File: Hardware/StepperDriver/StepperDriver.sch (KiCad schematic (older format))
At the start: 13 parts, among them M1A CONN_01X02, Q1 FQP20N06, Q2 FQP20N06, Q3 FQP20N06, Q4 FQP20N06, Q5 BC547, Q6 BC547, U1 74HC00

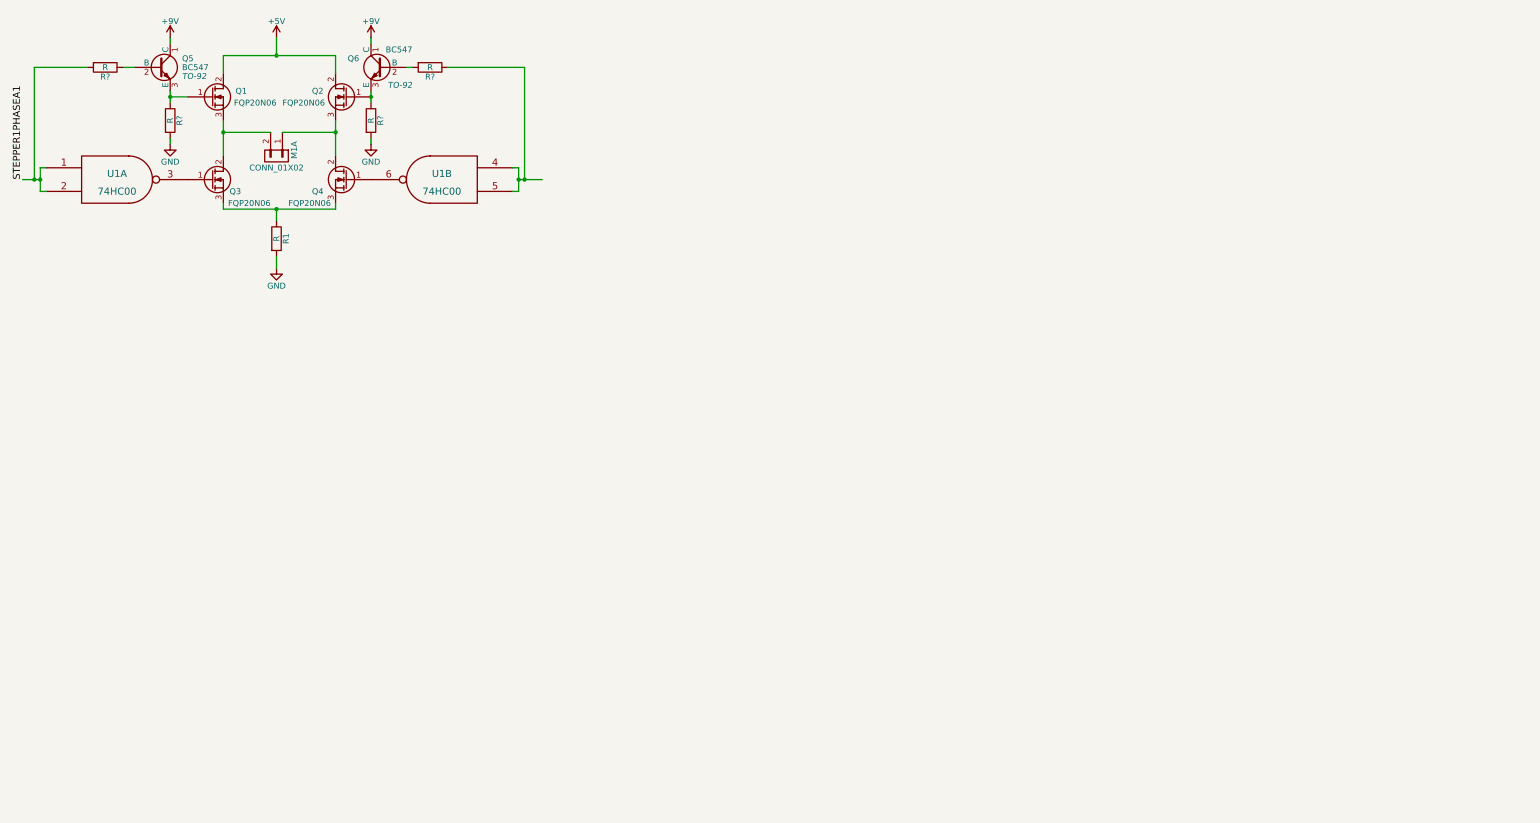
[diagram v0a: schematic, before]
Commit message: updated schematic for 2 motors
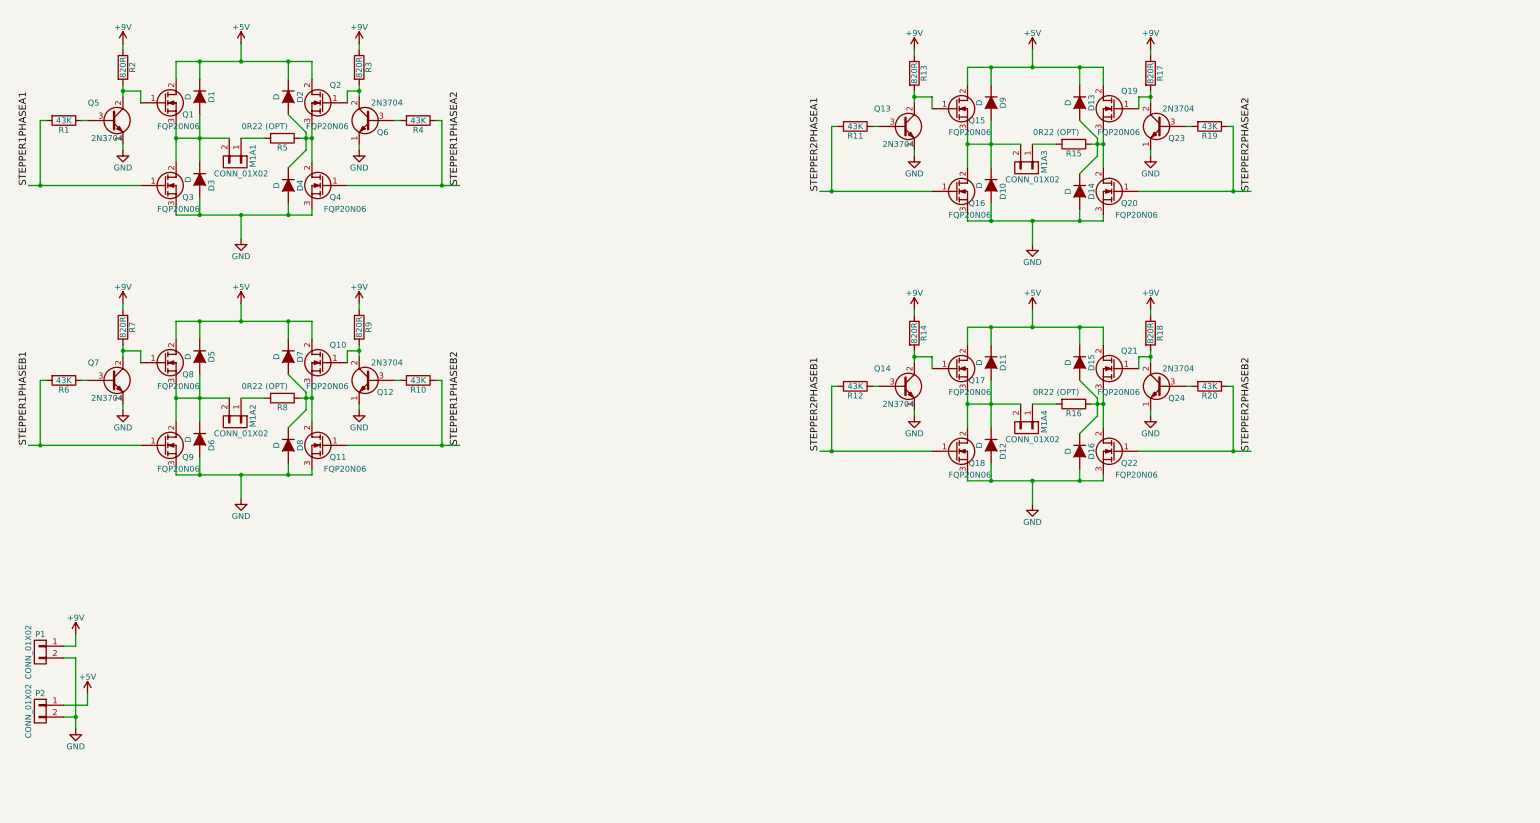
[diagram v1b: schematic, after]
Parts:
- removed Q5, Q6: BC547, TO-92, symbol BC547
- removed U1: 74HC00, symbol 74HC00
- added D1, D10, D11, D12, D13, D14, D15, D16, D2, D3, D4, D5, D6, D7, D8, D9: D, symbol D
- added M1A2, M1A3, M1A4, P1, P2: CONN_01X02, symbol CONN_01X02
- added Q10, Q11, Q15, Q16, Q17, Q18, Q19, Q20, Q21, Q22, Q8, Q9: FQP20N06, symbol Q_NMOS_GDS
- added Q12, Q13, Q14, Q23, Q24, Q5, Q6, Q7: 2N3704, symbol Q_NPN_ECB
- added R10, R11, R12, R19, R20, R6: 43K, symbol R
- added R13, R14, R17, R18, R7, R9: 820R, symbol R
- added R15, R16, R8: 0R22 (OPT), symbol R
- R1, R4: renamed from R?; value R -> 43K
- R2, R3: renamed from R?; value R -> 820R
- R5: renamed from R1; value R -> 0R22 (OPT)
- renumbered M1A to M1A1
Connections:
- net +5V: now also D1.1 (K), D11.1 (K), D13.1 (K), D15.1 (K), D2.1 (K), D5.1 (K), D7.1 (K), D9.1 (K), P2.1 (P1), Q10.2 (D), Q15.2 (D), Q17.2 (D), Q19.2 (D), Q21.2 (D), Q8.2 (D)
- net +9V: now also R2.1, R3.1, P1.1 (P1), R13.1, R14.1, R17.1, R18.1, R7.1, R9.1
- net GND: now also Q3.3 (S), Q4.3 (S), D10.2 (A), D12.2 (A), D14.2 (A), D16.2 (A), D3.2 (A), D4.2 (A), D6.2 (A), D8.2 (A), P1.2 (P2), P2.2 (P2), Q11.3 (S), Q12.1 (E), Q13.1 (E), Q14.1 (E), Q16.3 (S), Q18.3 (S), Q20.3 (S), Q22.3 (S), Q23.1 (E), Q24.1 (E), Q5.1 (E), Q6.1 (E), Q7.1 (E), Q9.3 (S); no longer R2.2, R3.2, R5.2
- net STEPPER1PHASEA1: now also Q3.1 (G)
- net at Q1.1 (G): now also R2.2, Q5.2 (C); no longer R2.1
- net at M1A1.2 (P2), Q1.3 (S), Q3.2 (D): now also D1.2 (A), D3.1 (K)
- net at Q2.1 (G): now also R3.2, Q6.2 (C); no longer R3.1
- net at Q2.3 (S), Q4.2 (D): now also R5.1, D2.2 (A), D4.1 (K); no longer M1A1.1 (P1)
- net STEPPER1PHASEA2: now reaches Q4.1 (G)
- net STEPPER1PHASEA2: now also R4.1
- net at R1.1: now also Q5.3 (B)
- net at R4.2: now also Q6.3 (B)
- new net: M1A1.1 (P1), R5.2
- new net: Q7.2 (C), Q8.1 (G), R7.2
- new net: D5.2 (A), D6.1 (K), M1A2.2 (P2), Q8.3 (S), Q9.2 (D)
- new net: Q10.1 (G), Q12.2 (C), R9.2
- new net: D7.2 (A), D8.1 (K), Q10.3 (S), Q11.2 (D), R8.1
- new net: M1A2.1 (P1), R8.2
- new net: Q7.3 (B), R6.1
- new net: Q12.3 (B), R10.2
- new net: Q13.2 (C), Q15.1 (G), R13.2
- new net: D10.1 (K), D9.2 (A), M1A3.2 (P2), Q15.3 (S), Q16.2 (D)
- new net: Q19.1 (G), Q23.2 (C), R17.2
- new net: D13.2 (A), D14.1 (K), Q19.3 (S), Q20.2 (D), R15.1
- new net: M1A3.1 (P1), R15.2
- new net: Q13.3 (B), R11.1
- new net: Q23.3 (B), R19.2
- new net: Q14.2 (C), Q17.1 (G), R14.2
- new net: D11.2 (A), D12.1 (K), M1A4.2 (P2), Q17.3 (S), Q18.2 (D)
- new net: Q21.1 (G), Q24.2 (C), R18.2
- new net: D15.2 (A), D16.1 (K), Q21.3 (S), Q22.2 (D), R16.1
- new net: M1A4.1 (P1), R16.2
- new net: Q14.3 (B), R12.1
- new net: Q24.3 (B), R20.2
- new net STEPPER1PHASEB1: Q9.1 (G), R6.2
- new net STEPPER1PHASEB2: Q11.1 (G), R10.1
- new net STEPPER2PHASEA1: Q16.1 (G), R11.2
- new net STEPPER2PHASEA2: Q20.1 (G), R19.1
- new net STEPPER2PHASEB1: Q18.1 (G), R12.2
- new net STEPPER2PHASEB2: Q22.1 (G), R20.1
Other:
- moved on the sheet: M1A1, Q1, Q2, Q3, Q4, R1, R2, R3, R4, R5

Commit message: added component values. Updated for 3 motor design
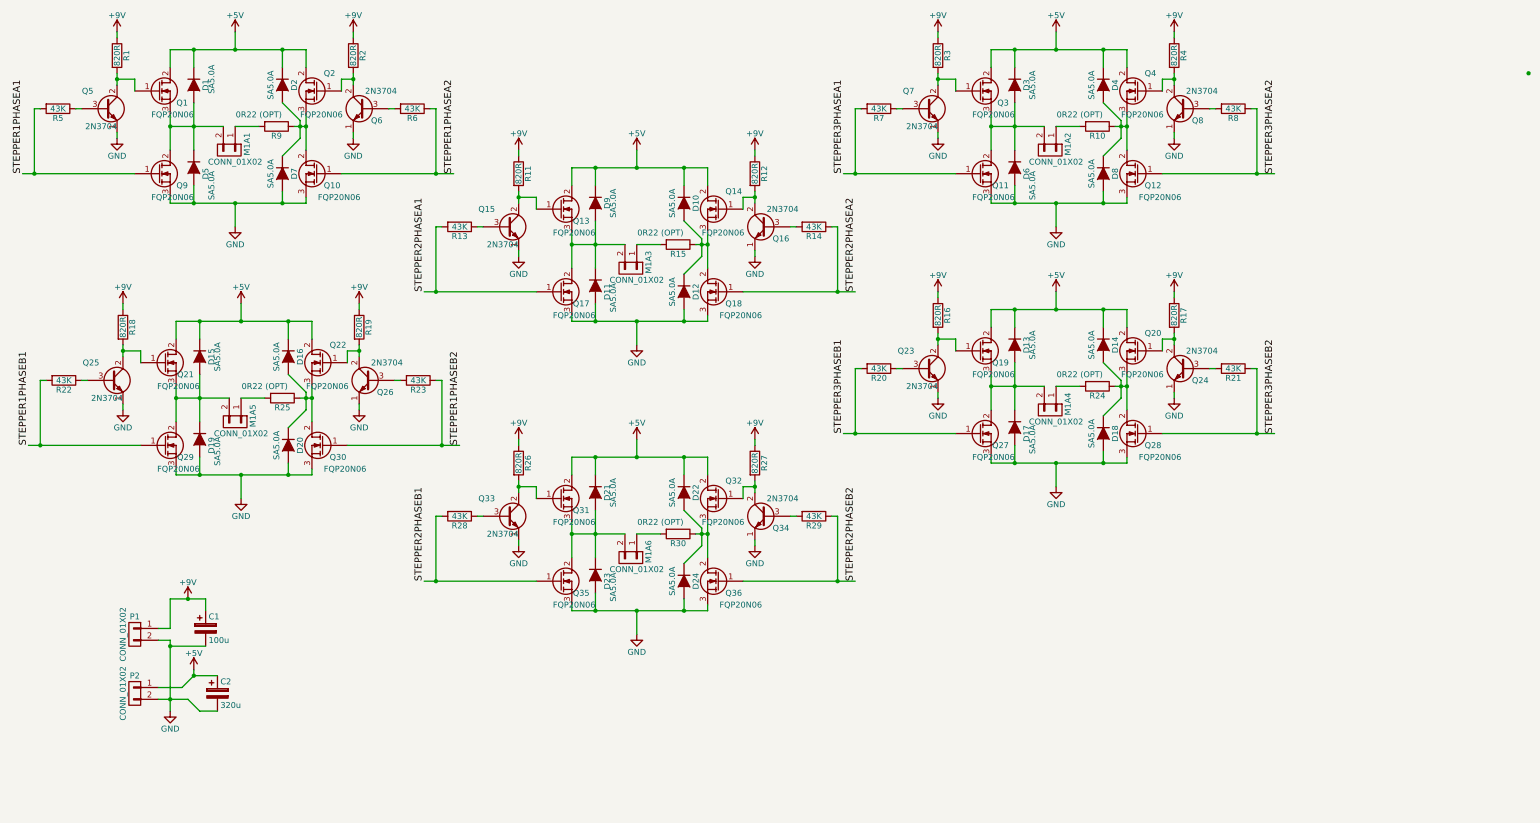
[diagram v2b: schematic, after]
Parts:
- added C1: 100u, symbol CP
- added C2: 320u, symbol CP
- added D10, D11, D12, D21, D22, D23, D24, D9: SA5.0A, symbol D
- added M1A3, M1A6: CONN_01X02, symbol CONN_01X02
- added Q13, Q14, Q17, Q18, Q31, Q32, Q35, Q36: FQP20N06, symbol Q_NMOS_GDS
- added Q15, Q16, Q33, Q34: 2N3704, symbol Q_NPN_ECB
- added R11, R12, R26, R27: 820R, symbol R
- added R13, R14, R28, R29: 43K, symbol R
- added R15, R30: 0R22 (OPT), symbol R
- D1, D2: value D -> SA5.0A
- D13: renamed from D11; value D -> SA5.0A
- D14: renamed from D15; value D -> SA5.0A
- D15: renamed from D5; value D -> SA5.0A
- D16: renamed from D7; value D -> SA5.0A
- D17: renamed from D12; value D -> SA5.0A
- D18: renamed from D16; value D -> SA5.0A
- D19: renamed from D6; value D -> SA5.0A
- D20: renamed from D8; value D -> SA5.0A
- D3: renamed from D9; value D -> SA5.0A
- D4: renamed from D13; value D -> SA5.0A
- D5: renamed from D3; value D -> SA5.0A
- D6: renamed from D10; value D -> SA5.0A
- D7: renamed from D4; value D -> SA5.0A
- D8: renamed from D14; value D -> SA5.0A
- renumbered M1A3 to M1A2, M1A2 to M1A5, Q4 to Q10, Q16 to Q11, Q20 to Q12, Q17 to Q19, Q21 to Q20, Q8 to Q21, Q10 to Q22, Q14 to Q23, Q7 to Q25, Q12 to Q26, Q18 to Q27, Q22 to Q28, Q9 to Q29, Q15 to Q3, Q11 to Q30, Q19 to Q4, Q13 to Q7, Q23 to Q8, Q3 to Q9, R2 to R1, R15 to R10, R14 to R16, R18 to R17, R7 to R18, R9 to R19, R3 to R2, R12 to R20, R20 to R21, R6 to R22, R10 to R23, R16 to R24, R8 to R25, R13 to R3, R17 to R4, R1 to R5, R4 to R6, R11 to R7, R19 to R8, R5 to R9
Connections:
- net +5V: now also C2.1, D10.1 (K), D21.1 (K), D22.1 (K), D9.1 (K), Q13.2 (D), Q14.2 (D), Q31.2 (D), Q32.2 (D)
- net +9V: now also C1.1, R11.1, R12.1, R26.1, R27.1
- net GND: now also C1.2, C2.2, D11.2 (A), D12.2 (A), D23.2 (A), D24.2 (A), Q15.1 (E), Q16.1 (E), Q17.3 (S), Q18.3 (S), Q33.1 (E), Q34.1 (E), Q35.3 (S), Q36.3 (S)
- net STEPPER2PHASEA1: now also Q17.1 (G), R13.2; no longer Q11.1 (G), R7.2
- net STEPPER2PHASEA2: now also Q18.1 (G), R14.1; no longer Q12.1 (G), R8.1
- net STEPPER2PHASEB1: now also Q35.1 (G), R28.2; no longer Q27.1 (G), R20.2
- net STEPPER2PHASEB2: now also Q36.1 (G), R29.1; no longer Q28.1 (G), R21.1
- new net: Q13.1 (G), Q15.2 (C), R11.2
- new net: D11.1 (K), D9.2 (A), M1A3.2 (P2), Q13.3 (S), Q17.2 (D)
- new net: Q14.1 (G), Q16.2 (C), R12.2
- new net: D10.2 (A), D12.1 (K), Q14.3 (S), Q18.2 (D), R15.1
- new net: M1A3.1 (P1), R15.2
- new net: Q15.3 (B), R13.1
- new net: Q16.3 (B), R14.2
- new net: Q31.1 (G), Q33.2 (C), R26.2
- new net: D21.2 (A), D23.1 (K), M1A6.2 (P2), Q31.3 (S), Q35.2 (D)
- new net: Q32.1 (G), Q34.2 (C), R27.2
- new net: D22.2 (A), D24.1 (K), Q32.3 (S), Q36.2 (D), R30.1
- new net: M1A6.1 (P1), R30.2
- new net: Q33.3 (B), R28.1
- new net: Q34.3 (B), R29.2
- new net STEPPER3PHASEA1: Q11.1 (G), R7.2
- new net STEPPER3PHASEA2: Q12.1 (G), R8.1
- new net STEPPER3PHASEB1: Q27.1 (G), R20.2
- new net STEPPER3PHASEB2: Q28.1 (G), R21.1
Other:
- moved on the sheet: D1, D13, D14, D17, D18, D2, D3, D4, D5, D6, D7, D8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

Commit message: added missing diode values, added motor connectors. Exported Schematic to PDF
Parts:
- added P3, P4, P5: CONN_01X04, symbol CONN_01X04
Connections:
- wire segments 254 -> 266

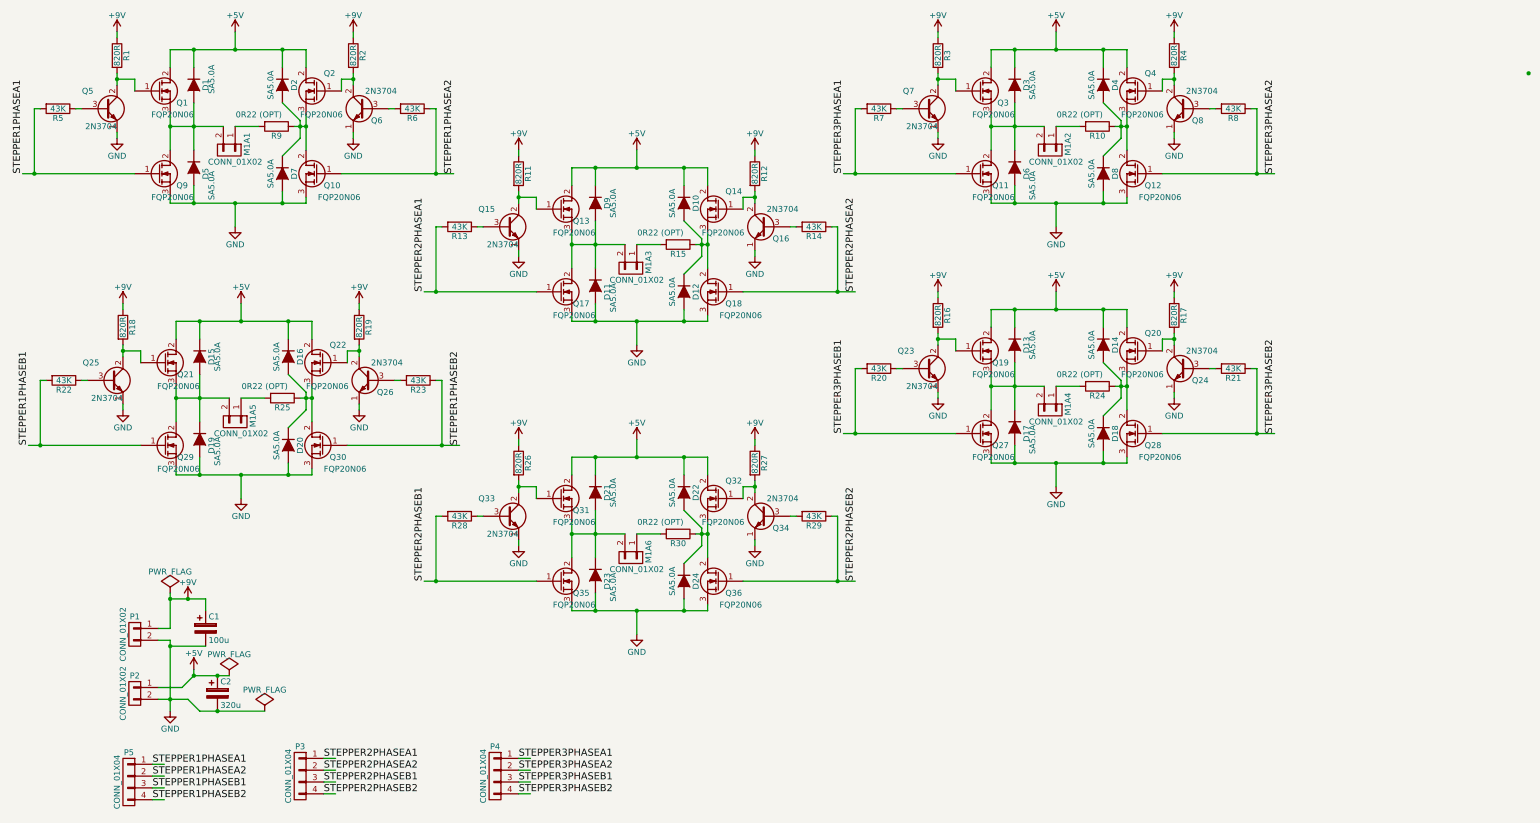
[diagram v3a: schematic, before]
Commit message: initial mockup of single channel driver
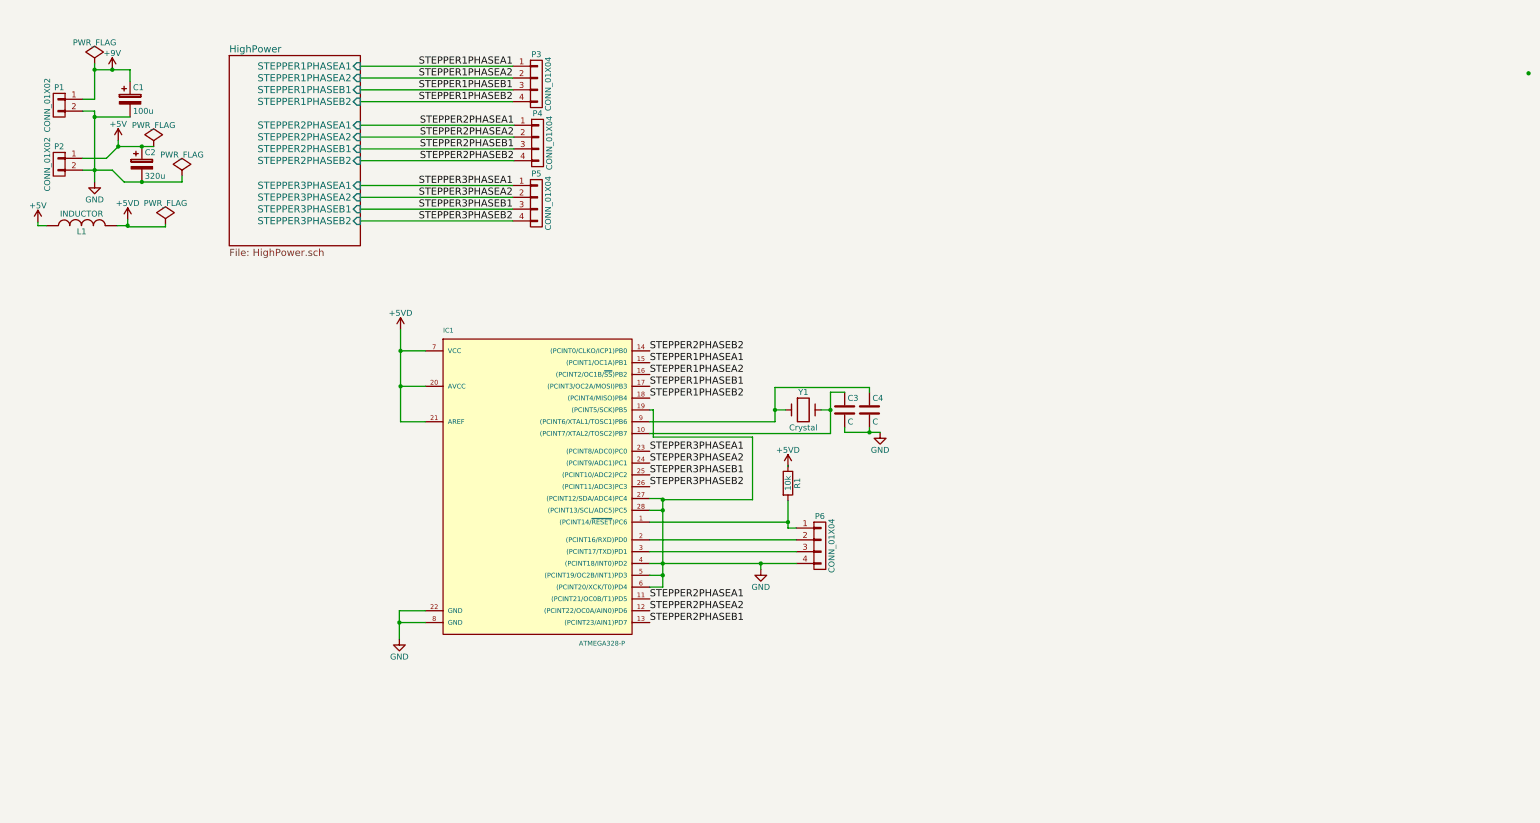
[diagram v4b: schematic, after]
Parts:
- removed D1, D10, D11, D12, D13, D14, D15, D16, D17, D18, D19, D2, D20, D21, D22, D23, D24, D3, D4, D5, D6, D7, D8, D9: SA5.0A, symbol D
- removed M1A1, M1A2, M1A3, M1A4, M1A5, M1A6: CONN_01X02, symbol CONN_01X02
- removed Q1, Q10, Q11, Q12, Q13, Q14, Q17, Q18, Q19, Q2, Q20, Q21, Q22, Q27, Q28, Q29, Q3, Q30, Q31, Q32, Q35, Q36, Q4, Q9: FQP20N06, symbol Q_NMOS_GDS
- removed Q15, Q16, Q23, Q24, Q25, Q26, Q33, Q34, Q5, Q6, Q7, Q8: 2N3704, symbol Q_NPN_ECB
- removed R10, R15, R24, R25, R30, R9: 0R22 (OPT), symbol R
- removed R11, R12, R16, R17, R18, R19, R2, R26, R27, R3, R4: 820R, symbol R
- removed R13, R14, R20, R21, R22, R23, R28, R29, R5, R6, R7, R8: 43K, symbol R
- added C3, C4: C, Capacitors_ThroughHole:C_Disc_D3_P2.5, symbol C
- added IC1: ATMEGA328-P, Housings_DIP:DIP-28_W7.62mm_LongPads, symbol ATMEGA328-P
- added L1: INDUCTOR, Inductors_NEOSID:Neosid_Inductor_Sd12k-style3, symbol INDUCTOR
- added P6: CONN_01X04, Terminal_Blocks:TerminalBlock_Pheonix_MPT-2.54mm_4pol, symbol CONN_01X04
- added Y1: Crystal, Crystals:Crystal_HC48-U_Vertical, symbol Crystal
- C1, C2: footprint (none) -> Capacitors_ThroughHole:C_Radial_D10_L20_P7.5
- P1, P2: footprint (none) -> Terminal_Blocks:TerminalBlock_Pheonix_MPT-2.54mm_2pol
- P3, P4, P5: footprint (none) -> Terminal_Blocks:TerminalBlock_Pheonix_MPT-2.54mm_4pol
- R1: value 820R -> 10k; footprint (none) -> Resistors_ThroughHole:Resistor_Horizontal_RM10mm
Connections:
- net labels added: +5VD
- wire segments 266 -> 70
